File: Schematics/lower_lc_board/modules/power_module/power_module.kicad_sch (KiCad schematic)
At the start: 29 parts, among them J1 Stack Male Edge Connector, U1 TVS3300DRV, U2 LD1117S33TR_SOT223, U3 ID_LM66100DCKR, U4 ID_LM66100DCKR

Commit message: pin assignments verified
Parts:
- added C44: 1uF, Capacitor_SMD:C_0603_1608Metric, symbol Device:C
- added U10: ID_LM66100DCKR, LM66100:SC-70-6, symbol QRET_Buck_PSU:LM66100DCKR
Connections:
- net +3V3: now also U10.3 (*CE), U10.6 (VOUT)
- net GND: now also C44.2, U10.2 (GND), U10.5 (ST)
- new net V_SWD: C44.1, U10.1 (VIN)
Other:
- moved on the sheet: C7, C8, D4, R4, TP6, U2

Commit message: start layout
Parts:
- R4: value 150 -> 330
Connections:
- net 3V3_USB: no longer R4.1
- net 5V_USB: now also R4.1
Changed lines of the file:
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@@
 	)
 	(junction
-		(at 208.28 137.16)
-		(diameter 0)
-		(color 0 0 0 0)
-	)
-	(junction
 		(at 172.72 134.62)
 		(diameter 0)
@@
 	(wire
 		(pts
-			(xy 208.28 137.16) (xy 220.98 137.16)
-		)
-		(stroke
-			(width 0)
-			(type default)
-		)
-	)
-	(wire
-		(pts
 			(xy 88.9 162.56) (xy 95.25 162.56)
 		)
@@
 	(wire
 		(pts
+			(xy 209.55 128.27) (xy 209.55 129.54)
+		)
+		(stroke
+			(width 0)
+			(type default)
+		)
+	)
+	(wire
+		(pts
 			(xy 176.53 76.2) (xy 172.72 76.2)
 		)
@@
 	(wire
 		(pts
-			(xy 199.39 137.16) (xy 208.28 137.16)
+			(xy 199.39 137.16) (xy 220.98 137.16)
 		)
 		(stroke
@@
 	(wire
 		(pts
-			(xy 208.28 135.89) (xy 208.28 137.16)
-		)
-		(stroke
-			(width 0)
-			(type default)
-		)
-	)
-	(wire
-		(pts
 			(xy 78.74 147.32) (xy 88.9 147.32)
 		)
@@
 		)
 	)
-	(text "Vf=2.6, R=150, I=4.7mA"
-		(exclude_from_sim no)
-		(at 213.36 118.11 0)
-		(effects
-			(font
-				(size 1.27 1.27)
-			)
-		)
-	)
 	(text "USB VBUS Regulation (->3V3)"
 		(exclude_from_sim no)
@@
 		)
 	)
+	(global_label "5V_USB"
+		(shape input)
+		(at 209.55 129.54 0)
+		(fields_autoplaced yes)
+		(effects
+			(font
+				(size 1.27 1.27)
+			)
+			(justify left)
+		)
+		(property "Intersheetrefs" "${INTERSHEET_REFS}"
+			(at 219.6109 129.54 0)
+			(effects
+				(font
+					(size 1.27 1.27)
+				)
+				(justify left)
+				(hide yes)
+			)
+		)
+	)
 	(symbol
 		(lib_id "QRET_Buck_PSU:LM66100DCKR")
@@
 	)
 	(symbol
+		(lib_id "Device:R")
+		(at 209.55 124.46 180)
+		(unit 1)
+		(exclude_from_sim no)
+		(in_bom yes)
+		(on_board yes)
+		(dnp no)
+		(property "Reference" "R4"
+			(at 208.28 124.46 0)
+			(effects
+				(font
+					(size 1.27 1.27)
+				)
+				(justify left)
+			)
+		)
+		(property "Value" "330"
+			(at 209.55 122.682 90)
+			(effects
+				(font
+					(size 1.27 1.27)
+				)
+				(justify left)
+			)
+		)
+		(property "Footprint" "Resistor_SMD:R_0603_1608Metric"
+			(at 211.328 124.46 90)
+			(effects
+				(font
+					(size 1.27 1.27)
+				)
+				(hide yes)
+			)
+		)
+		(property "Datasheet" "~"
+			(at 209.55 124.46 0)
+			(effects
+				(font
+					(size 1.27 1.27)
+				)
+				(hide yes)
+			)
+		)
+		(property "Description" "Resistor"
+			(at 209.55 124.46 0)
+			(effects
+				(font
+					(size 1.27 1.27)
+				)
+				(hide yes)
+			)
+		)
+		(property "LCSC" "C22808"
+			(at 209.55 124.46 90)
+			(effects
+				(font
+					(size 1.27 1.27)
+				)
+				(hide yes)
+			)
+		)
+		(pin "2"
+		)
+		(pin "1"
+		)
+		(instances
+			(project "lower_lc_board"
+				(path "/d63798c4-e363-437e-9012-e4aff32e6642/ea1dc739-d1f4-46a0-a090-2a1bf39da427"
+					(reference "R4")
+					(unit 1)
+				)
+			)
+		)
+	)
+	(symbol
 		(lib_id "power:GND")
 		(at 172.72 96.52 0)
@@
 	)
 	(symbol
-		(lib_id "Device:R")
-		(at 208.28 132.08 180)
+		(lib_id "Device:LED")
+		(at 213.36 120.65 180)
 		(unit 1)
 		(exclude_from_sim no)
@@
 		(on_board yes)
 		(dnp no)
-		(property "Reference" "R4"
-			(at 207.01 132.08 0)
+		(property "Reference" "D4"
+			(at 219.456 123.444 0)
 			(effects
 				(font
 					(size 1.27 1.27)
 				)
-				(justify left)
 			)
 		)
-		(property "Value" "150"
-			(at 208.28 130.81 90)
+		(property "Value" "USB_LED (GRN)"
+			(at 219.456 125.984 0)
 			(effects
 				(font
 					(size 1.27 1.27)
 				)
-				(justify left)
 			)
 		)
-		(property "Footprint" "Resistor_SMD:R_0603_1608Metric"
-			(at 210.058 132.08 90)
+		(property "Footprint" "LED_SMD:LED_0805_2012Metric"
+			(at 213.36 120.65 0)
 			(effects
 				(font
@@
 		)
 		(property "Datasheet" "~"
-			(at 208.28 132.08 0)
+			(at 213.36 120.65 0)
 			(effects
 				(font
@@
 			)
 		)
-		(property "Description" "Resistor"
-			(at 208.28 132.08 0)
+		(property "Description" "Light emitting diode"
+			(at 213.36 120.65 0)
 			(effects
 				(font
@@
 			)
 		)
-		(property "LCSC" "C22808"
-			(at 208.28 132.08 90)
+		(property "LCSC" "C2297"
+			(at 213.36 120.65 0)
 			(effects
 				(font
@@
 			(project "lower_lc_board"
 				(path "/d63798c4-e363-437e-9012-e4aff32e6642/ea1dc739-d1f4-46a0-a090-2a1bf39da427"
-					(reference "R4")
+					(reference "D4")
 					(unit 1)
 				)
@@
 	)
 	(symbol
+		(lib_id "power:GND")
+		(at 217.17 120.65 90)
+		(unit 1)
+		(exclude_from_sim no)
+		(in_bom yes)
+		(on_board yes)
+		(dnp no)
+		(property "Reference" "#PWR017"
+			(at 223.52 120.65 0)
+			(effects
+				(font
+					(size 1.27 1.27)
+				)
+				(hide yes)
+			)
+		)
+		(property "Value" "GND"
+			(at 220.218 120.65 90)
+			(effects
+				(font
+					(size 1.27 1.27)
+				)
+				(justify right)
+			)
+		)
+		(property "Footprint" ""
+			(at 217.17 120.65 0)
+			(effects
+				(font
+					(size 1.27 1.27)
+				)
+				(hide yes)
+			)
+		)
+		(property "Datasheet" ""
+			(at 217.17 120.65 0)
+			(effects
+				(font
+					(size 1.27 1.27)
+				)
+				(hide yes)
+			)
+		)
+		(property "Description" "Power symbol creates a global label with name \"GND\" , ground"
+			(at 217.17 120.65 0)
+			(effects
+				(font
+					(size 1.27 1.27)
+				)
+				(hide yes)
+			)
+		)
+		(pin "1"
+		)
+		(instances
+			(project "lower_lc_board"
+				(path "/d63798c4-e363-437e-9012-e4aff32e6642/ea1dc739-d1f4-46a0-a090-2a1bf39da427"
+					(reference "#PWR017")
+					(unit 1)
+				)
+			)
+		)
+	)
+	(symbol
 		(lib_id "power:+3V3")
 		(at 227.33 45.72 270)
@@
 	)
 	(symbol
-		(lib_id "Device:LED")
-		(at 212.09 128.27 180)
-		(unit 1)
-		(exclude_from_sim no)
-		(in_bom yes)
-		(on_board yes)
-		(dnp no)
-		(property "Reference" "D4"
-			(at 212.598 121.666 0)
-			(effects
-				(font
-					(size 1.27 1.27)
-				)
-			)
-		)
-		(property "Value" "USB_LED (GRN)"
-			(at 212.598 124.206 0)
-			(effects
-				(font
-					(size 1.27 1.27)
-				)
-			)
-		)
-		(property "Footprint" "LED_SMD:LED_0805_2012Metric"
-			(at 212.09 128.27 0)
-			(effects
-				(font
-					(size 1.27 1.27)
-				)
-				(hide yes)
-			)
-		)
-		(property "Datasheet" "~"
-			(at 212.09 128.27 0)
-			(effects
-				(font
-					(size 1.27 1.27)
-				)
-				(hide yes)
-			)
-		)
-		(property "Description" "Light emitting diode"
-			(at 212.09 128.27 0)
-			(effects
-				(font
-					(size 1.27 1.27)
-				)
-				(hide yes)
-			)
-		)
-		(property "LCSC" "C2297"
-			(at 212.09 128.27 0)
-			(effects
-				(font
-					(size 1.27 1.27)
-				)
-				(hide yes)
-			)
-		)
-		(pin "2"
-		)
-		(pin "1"
-		)
-		(instances
-			(project "lower_lc_board"
-				(path "/d63798c4-e363-437e-9012-e4aff32e6642/ea1dc739-d1f4-46a0-a090-2a1bf39da427"
-					(reference "D4")
-					(unit 1)
-				)
-			)
-		)
-	)
-	(symbol
 		(lib_id "power:GND")
 		(at 190.5 146.05 0)
@@
 					(unit 1)
 				)
-			)
-		)
-	)
-	(symbol
-		(lib_id "power:GND")
-		(at 215.9 128.27 90)
-		(unit 1)
-		(exclude_from_sim no)
-		(in_bom yes)
-		(on_board yes)
-		(dnp no)
-		(property "Reference" "#PWR017"
-			(at 222.25 128.27 0)
-			(effects
-				(font
-					(size 1.27 1.27)
-				)
-				(hide yes)
-			)
-		)
-		(property "Value" "GND"
-			(at 218.948 128.27 90)
-			(effects
-				(font
-					(size 1.27 1.27)
-				)
-				(justify right)
-			)
-		)
-		(property "Footprint" ""
-			(at 215.9 128.27 0)
-			(effects
-				(font
-					(size 1.27 1.27)
-				)
-				(hide yes)
-			)
-		)
-		(property "Datasheet" ""
-			(at 215.9 128.27 0)
-			(effects
-				(font
-					(size 1.27 1.27)
-				)
-				(hide yes)
-			)
-		)
-		(property "Description" "Power symbol creates a global label with name \"GND\" , ground"
-			(at 215.9 128.27 0)
-			(effects
-				(font
-					(size 1.27 1.27)
-				)
-				(hide yes)
-			)
-		)
-		(pin "1"
-		)
-		(instances
-			(project "lower_lc_board"
-				(path "/d63798c4-e363-437e-9012-e4aff32e6642/ea1dc739-d1f4-46a0-a090-2a1bf39da427"
-					(reference "#PWR017")
-					(unit 1)
-				)

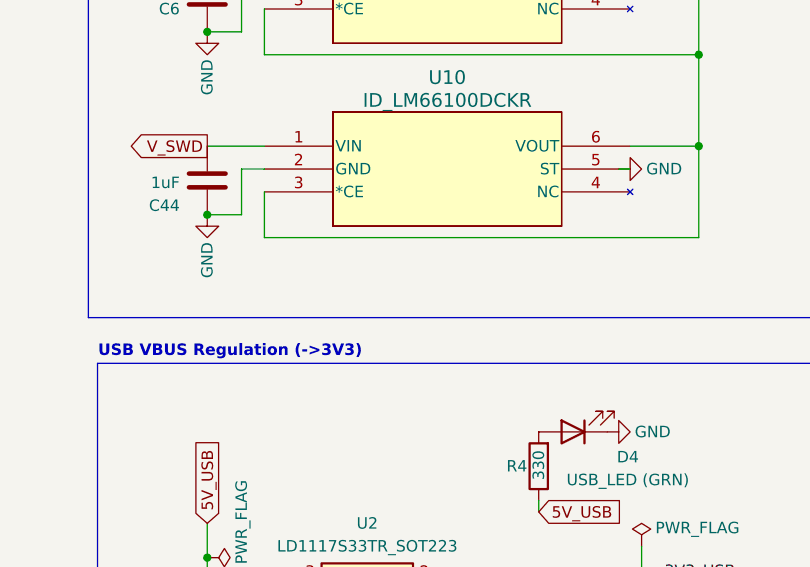
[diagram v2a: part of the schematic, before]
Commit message: layout work
#TODO
- smaller 3V3 buck, add HF cap
- finish layout
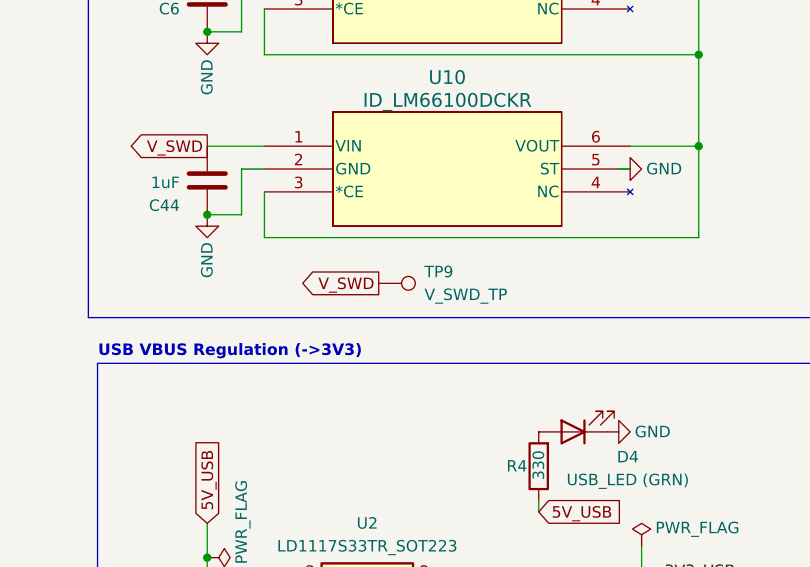
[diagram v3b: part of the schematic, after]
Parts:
- added TP9: V_SWD_TP, TestPoint:TestPoint_Pad_D1.0mm, symbol Connector:TestPoint
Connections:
- net V_SWD: now also TP9.1
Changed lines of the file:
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@@
+		)
+	)
+	(global_label "V_SWD"
+		(shape output)
+		(at 191.77 104.14 180)
+		(fields_autoplaced yes)
+		(effects
+			(font
+				(size 1.27 1.27)
+			)
+			(justify right)
+		)
+		(property "Intersheetrefs" "${INTERSHEET_REFS}"
+			(at 182.7977 104.14 0)
+			(effects
+				(font
+					(size 1.27 1.27)
+				)
+				(justify right)
+				(hide yes)
+			)
 		)
 	)
@@
 					(unit 1)
 				)
+			)
+		)
+	)
+	(symbol
+		(lib_id "Connector:TestPoint")
+		(at 191.77 104.14 270)
+		(unit 1)
+		(exclude_from_sim no)
+		(in_bom yes)
+		(on_board yes)
+		(dnp no)
+		(fields_autoplaced yes)
+		(property "Reference" "TP9"
+			(at 196.85 102.8699 90)
+			(effects
+				(font
+					(size 1.27 1.27)
+				)
+				(justify left)
+			)
+		)
+		(property "Value" "V_SWD_TP"
+			(at 196.85 105.4099 90)
+			(effects
+				(font
+					(size 1.27 1.27)
+				)
+				(justify left)
+			)
+		)
+		(property "Footprint" "TestPoint:TestPoint_Pad_D1.0mm"
+			(at 191.77 109.22 0)
+			(effects
+				(font
+					(size 1.27 1.27)
+				)
+				(hide yes)
+			)
+		)
+		(property "Datasheet" "~"
+			(at 191.77 109.22 0)
+			(effects
+				(font
+					(size 1.27 1.27)
+				)
+				(hide yes)
+			)
+		)
+		(property "Description" "test point"
+			(at 191.77 104.14 0)
+			(effects
+				(font
+					(size 1.27 1.27)
+				)
+				(hide yes)
+			)
+		)
+		(pin "1"
+		)
+		(instances
+			(project ""
+				(path "/d63798c4-e363-437e-9012-e4aff32e6642/ea1dc739-d1f4-46a0-a090-2a1bf39da427"
+					(reference "TP9")
+					(unit 1)
+				)

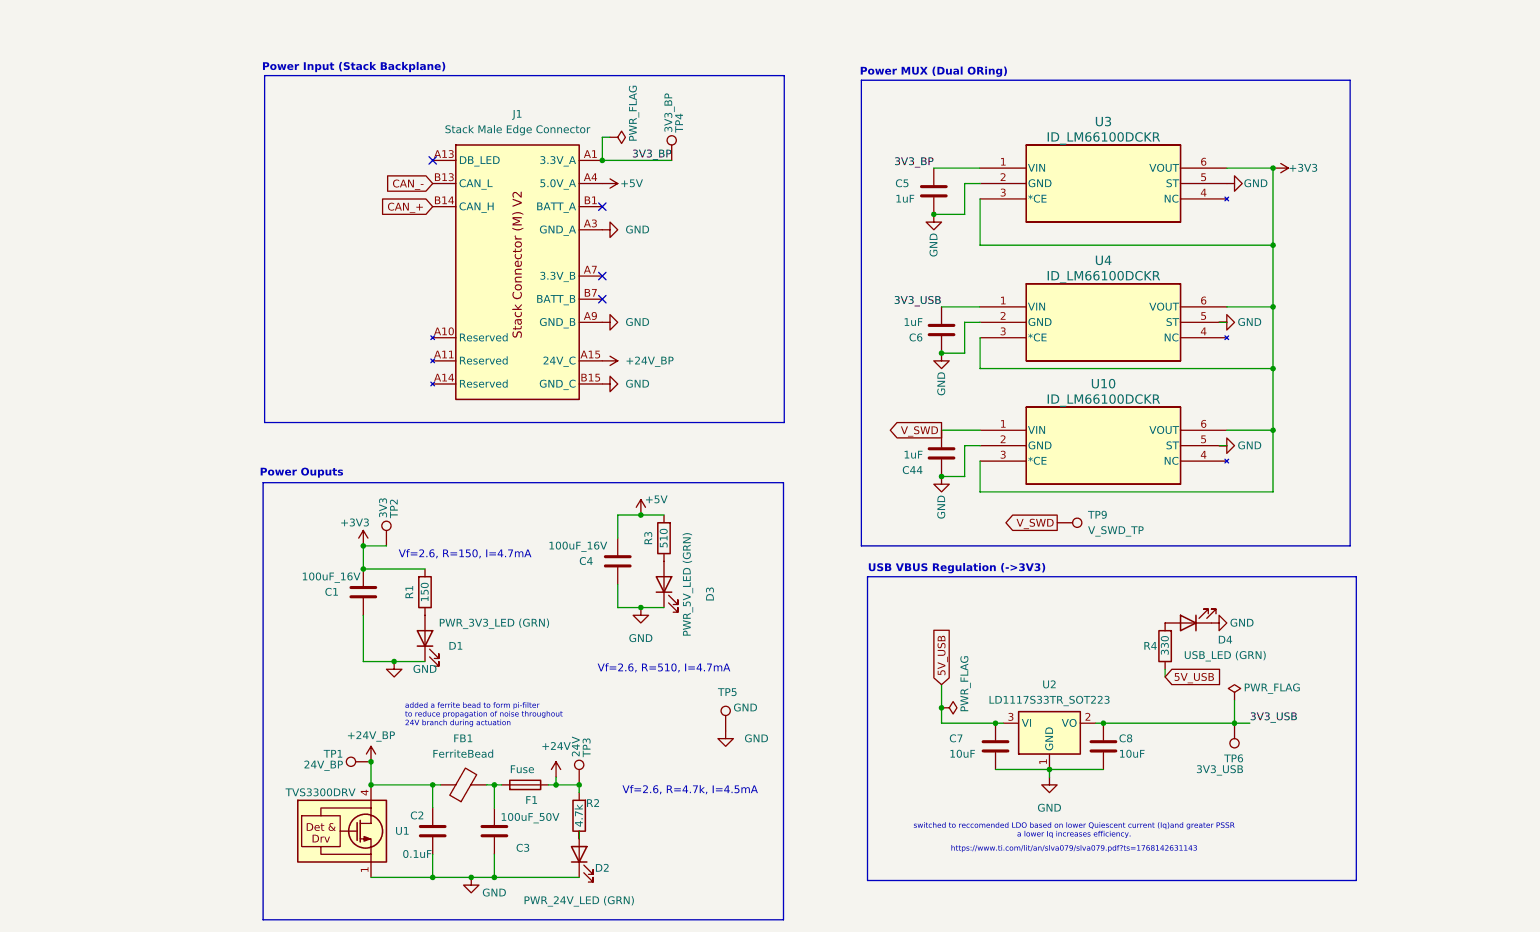
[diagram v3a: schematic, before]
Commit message: finish layout
- model paths need to be fixed
- waiting for confirmation for shared folders
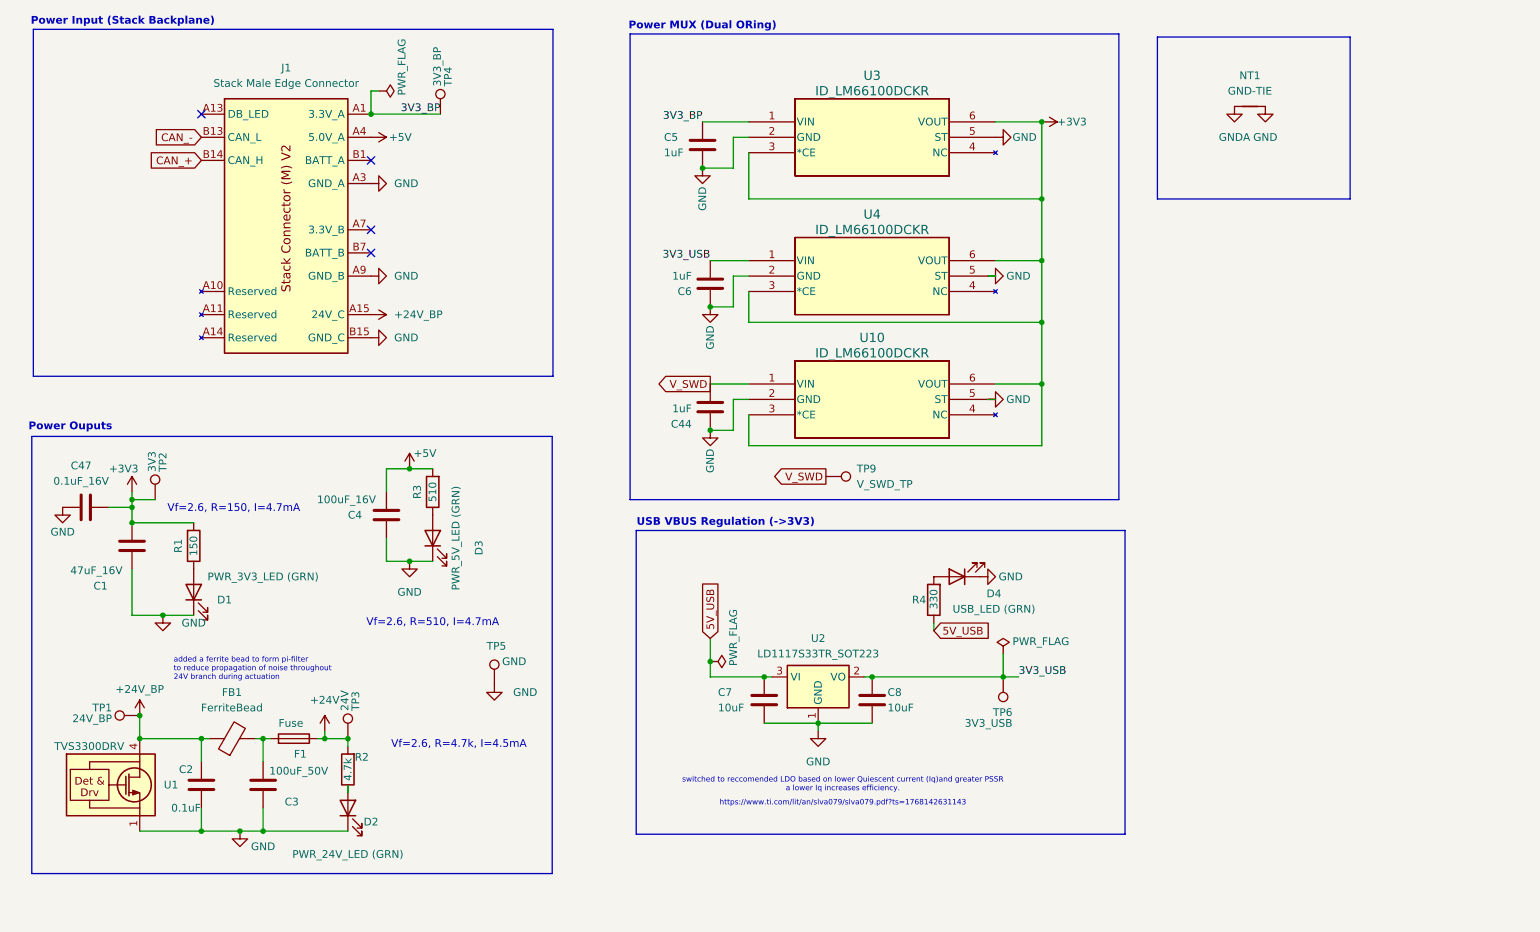
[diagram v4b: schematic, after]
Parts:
- added C47: 0.1uF_16V, Capacitor_SMD:C_0603_1608Metric, symbol Device:C
- added NT1: GND-TIE, NetTie:NetTie-2_SMD_Pad0.5mm, symbol Device:NetTie_2
- C1: value 100uF_16V -> 47uF_16V; footprint Capacitor_SMD:CP_Elec_6.3x5.9 -> Capacitor_SMD:C_1206_3216Metric
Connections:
- net +3V3: now also C47.2
- net GND: now also C47.1, NT1.2
- new net GNDA: NT1.1
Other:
- moved on the sheet: C1, C2, C3, C4, C44, C5, C6, C7, C8, D1, D2, D3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

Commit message: more layout work, add testing code
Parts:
- U2: value LD1117S33TR_SOT223 -> AMS1117; symbol Regulator_Linear:LD1117S33TR_SOT223 -> Regulator_Linear:AMS1117
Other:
- note removed: "https://www.ti.com/lit/an/slva079/slva079.pdf?ts=1768142631143"
- note removed: "switched to reccomended LDO based on lower Quiescent current (Iq)and greater PSSR a lower Iq increases efficiency."
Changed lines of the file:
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@@
 		)
 	)
-	(text "switched to reccomended LDO based on lower Quiescent current (Iq)and greater PSSR\na lower Iq increases efficiency.\n"
-		(exclude_from_sim no)
-		(at 156.464 147.32 0)
-		(effects
-			(font
-				(size 0.889 0.889)
-				(color 0 0 0 1)
-			)
-		)
-	)
-	(text "https://www.ti.com/lit/an/slva079/slva079.pdf?ts=1768142631143"
-		(exclude_from_sim no)
-		(at 156.464 150.368 0)
-		(effects
-			(font
-				(size 0.889 0.889)
-			)
-			(href "https://www.ti.com/lit/an/slva079/slva079.pdf?ts=1768142631143")
-		)
-	)
 	(text "Vf=2.6, R=150, I=4.7mA"
 		(exclude_from_sim no)
@@
 	)
 	(symbol
-		(lib_id "Regulator_Linear:LD1117S33TR_SOT223")
+		(lib_id "Regulator_Linear:AMS1117")
 		(at 152.4 129.54 0)
 		(unit 1)
@@
 			)
 		)
-		(property "Value" "LD1117S33TR_SOT223"
+		(property "Value" "AMS1117"
 			(at 152.4 125.73 0)
 			(effects
@@
 			)
 		)
-		(property "Datasheet" "${KIPRJMOD}/../../Datasheets/LDO-ld1117.pdf"
+		(property "Datasheet" "http://www.advanced-monolithic.com/pdf/ds1117.pdf"
 			(at 154.94 135.89 0)
 			(effects
@@
 			)
 		)
-		(property "Description" "800mA Fixed Low Drop Positive Voltage Regulator, Fixed Output 3.3V, SOT-223"
+		(property "Description" "1A Low Dropout regulator, positive, adjustable output, SOT-223"
 			(at 152.4 129.54 0)
 			(effects

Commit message: some routing work
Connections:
- net CAN_+ renamed CAN_P
- net CAN_- renamed CAN_N
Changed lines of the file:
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@@
 		)
 	)
-	(global_label "CAN_-"
+	(global_label "CAN_N"
 		(shape input)
 		(at 50.8 40.64 180)
@@
 		)
 		(property "Intersheetrefs" "${INTERSHEET_REFS}"
-			(at 41.5857 40.64 0)
+			(at 41.8276 40.64 0)
 			(effects
 				(font
@@
 		)
 	)
-	(global_label "CAN_+"
+	(global_label "CAN_P"
 		(shape input)
 		(at 50.8 44.45 180)
@@
 		)
 		(property "Intersheetrefs" "${INTERSHEET_REFS}"
-			(at 41.5857 44.45 0)
+			(at 41.8881 44.45 0)
 			(effects
 				(font

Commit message: organizational work
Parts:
- C1: value 47uF_16V -> 47uF
- C2: JLCPCB (none) -> C14663
- C3: value 100uF_50V -> 100uF
- C4: value 100uF_16V -> 100uF
- C44, C5, C6: JLCPCB (none) -> C15849
- C47: value 0.1uF_16V -> 0.1uF
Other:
- note added: "24V-LED: Vf=2.6, R=4.7k, I=4.5mA"
- note added: "3V3-LED: Vf=2.6, R=150, I=4.7mA"
- note added: "5V-LED: Vf=2.6, R=510, I=4.7mA"
- note added: "Analog GND Tie"
- note added: "PI-filter for filtering"
- note added: "Power LED Calculations"
- note added: "Power MUX (Triple ORing)"
- note removed: "Power MUX (Dual ORing)"
- note removed: "Vf=2.6, R=150, I=4.7mA"
- note removed: "Vf=2.6, R=4.7k, I=4.5mA"
- note removed: "Vf=2.6, R=510, I=4.7mA"
- note removed: "added a ferrite bead to form pi-filter to reduce propagation of noise throughout 24V branch during actuation"
- moved on the sheet: C1, C2, C3, C4, C44, C47, C5, C6, C7, C8, D1, D2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
